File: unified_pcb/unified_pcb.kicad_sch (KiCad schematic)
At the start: 100 parts, among them J1 Conn_01x02_Socket, J2 USB_C_Receptacle, J3 Conn_01x02_Socket, J4 Conn_01x03_Pin, Q1 Q_Photo_NPN, Q2 Q_Photo_NPN, Q3 Q_Photo_NPN, SW1 SW_Push, SW2 SW_Push, U1 BQ27421YZFR-G1A, U10 3.3V LDO, U11 LMD4030T261-OA1, U2 USBLC6-2P6, U4 RP2350_60QFN, U5 TLV7113318DDSER, U6 LP28013HQVF-435, U7 QSPI Flash, U8 TPGLF72101CSP4, U9 ICM-20948, Y1 12MHz

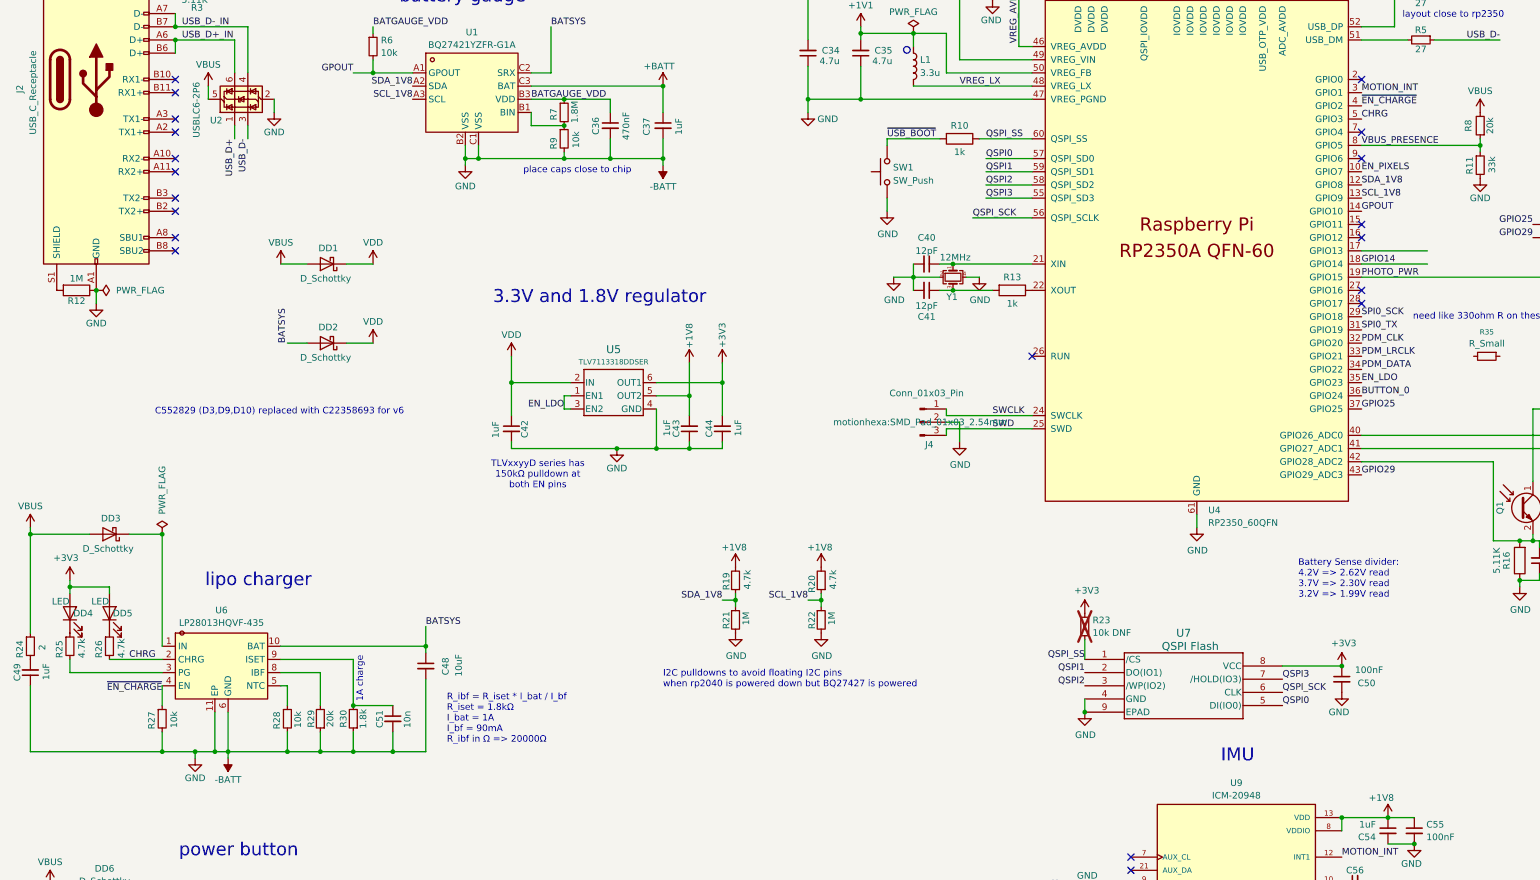
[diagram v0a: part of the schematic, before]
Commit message: switch to LY4176D charger
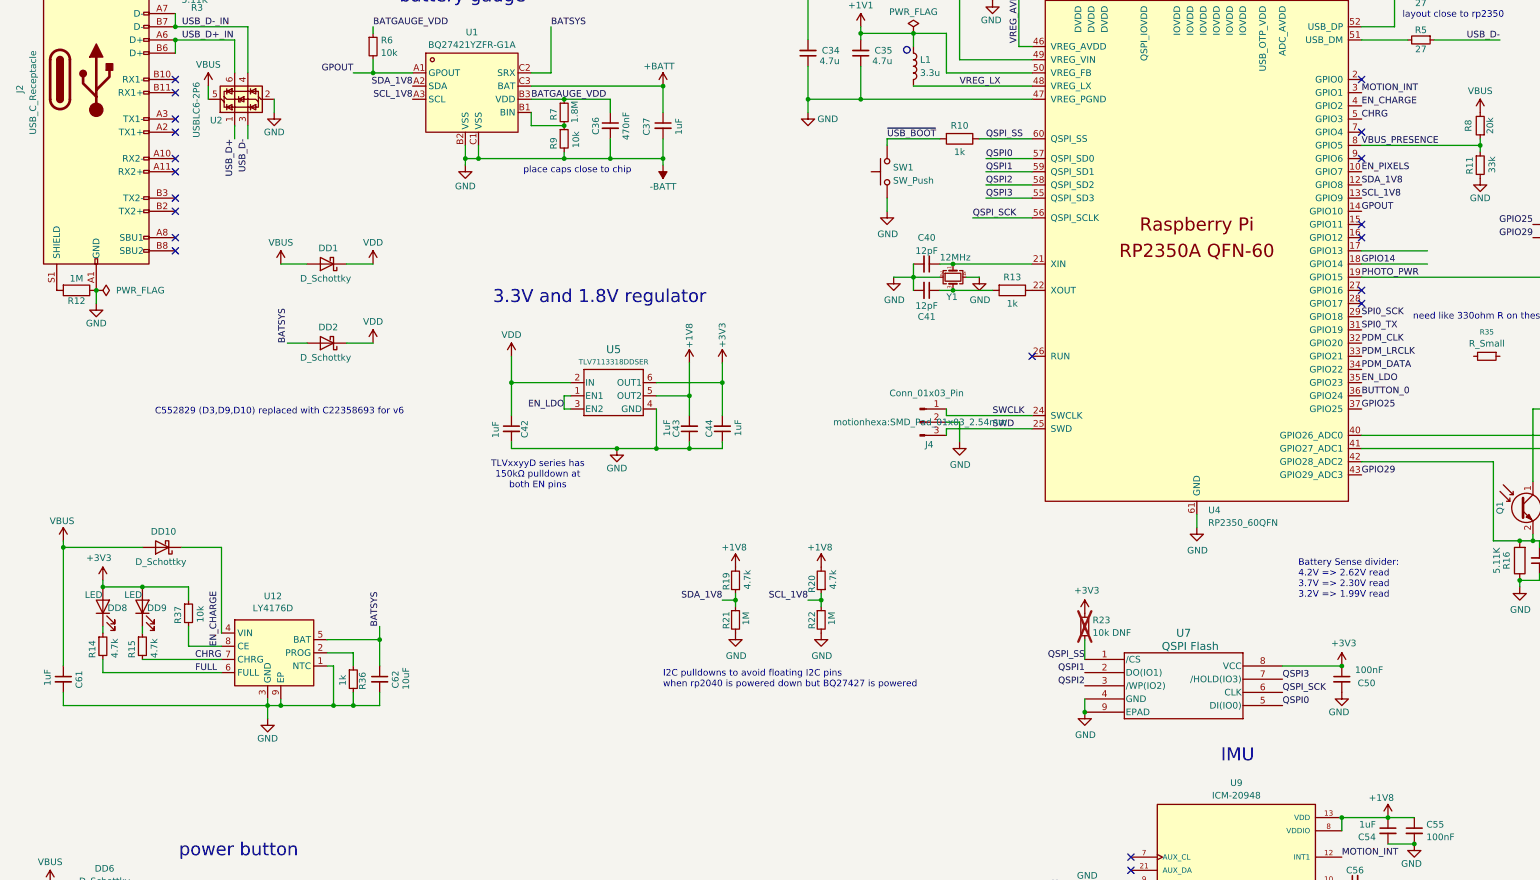
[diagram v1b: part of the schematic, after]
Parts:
- removed C48: 10uF, Capacitor_SMD:C_0603_1608Metric, symbol Device:C_Small
- removed C49: 1uF, Capacitor_SMD:C_0402_1005Metric, symbol Device:C_Small
- removed C51: 10n, Capacitor_SMD:C_0402_1005Metric, symbol Device:C_Small
- removed DD3: D_Schottky, motionhexa:DFN1608D-2, symbol Device:D_Schottky
- removed DD4, DD5: LED, LED_SMD:LED_0402_1005Metric, symbol Device:LED
- removed R24: 2, Resistor_SMD:R_0402_1005Metric, symbol Device:R_Small
- removed R25, R26: 4.7k, Resistor_SMD:R_0402_1005Metric, symbol Device:R_Small
- removed R27, R28: 10k, Resistor_SMD:R_0402_1005Metric, symbol Device:R_Small
- removed R29: 20k, Resistor_SMD:R_0402_1005Metric, symbol Device:R_Small
- removed R30: 1.8k, Resistor_SMD:R_0402_1005Metric, symbol Device:R_Small
- removed U6: LP28013HQVF-435, motionhexa:TDFN-10_L3.0-W3.0-P0.50-BL-EP, symbol motionhexa:LP28013HQVF-435
- added C61: 1uF, Capacitor_SMD:C_0402_1005Metric, symbol Device:C_Small
- added C62: 10uF, Capacitor_SMD:C_0603_1608Metric, symbol Device:C_Small
- added DD10: D_Schottky, motionhexa:DFN1608D-2, symbol Device:D_Schottky
- added DD8, DD9: LED, LED_SMD:LED_0402_1005Metric, symbol Device:LED
- added R14, R15: 4.7k, Resistor_SMD:R_0402_1005Metric, symbol Device:R_Small
- added R36: 1k, Resistor_SMD:R_0402_1005Metric, symbol Device:R_Small
- added R37: 10k, Resistor_SMD:R_0402_1005Metric, symbol Device:R_Small
- added U12: LY4176D, Package_DFN_QFN:DFN-8-1EP_2x2mm_P0.5mm_EP0.6x1.2mm, symbol motionhexa:LY4176D
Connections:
- net +3V3: now also DD8.2 (A), DD9.2 (A), R37.1
- net -BATT: now also C61.2, C62.2, R36.2, U12.1 (NTC), U12.3 (GND), U12.9 (EP)
- net BATSYS: now also C62.1, U12.5 (BAT)
- net CHRG: now also R15.2, U12.7 (CHRG)
- net VBUS: now also C61.1, DD10.2 (A)
- net ~{EN_CHARGE} renamed EN_CHARGE
- net EN_CHARGE: now also R37.2, U12.8 (CE)
- new net: DD9.1 (K), R15.1
- new net: DD10.1 (K), U12.4 (VIN)
- new net: DD8.1 (K), R14.1
- new net: R36.1, U12.2 (PROG)
- new net FULL: R14.2, U12.6 (FULL)
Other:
- note removed: "1A charge"
- note removed: "R_ibf = R_iset * I_bat / I_bf R_iset = 1.8kΩ I_bat = 1A I_bf = 90mA R_ibf in Ω => 20000Ω"
- note removed: "lipo charger"

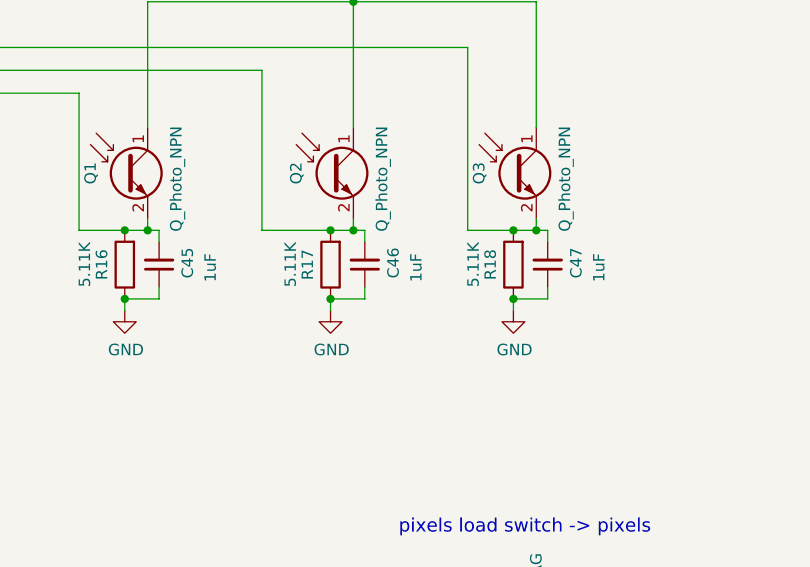
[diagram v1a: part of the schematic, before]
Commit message: phototransistor caps to 470nF for faster sampling
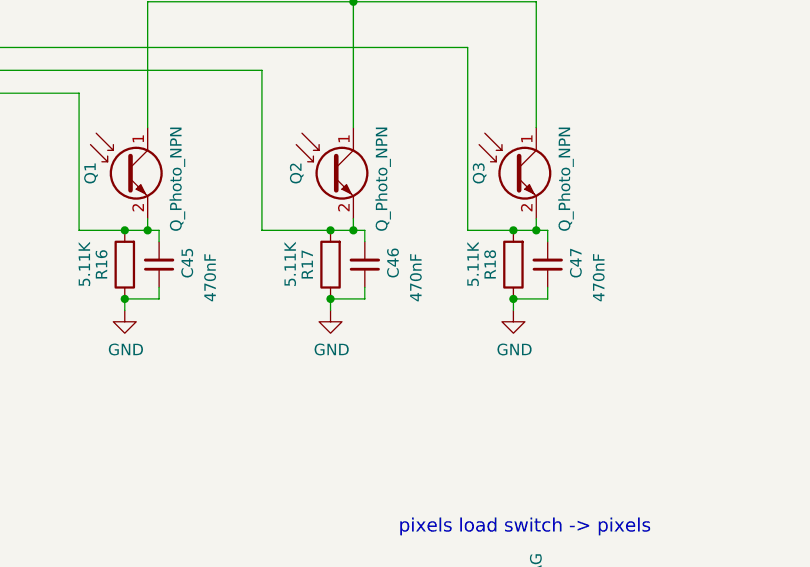
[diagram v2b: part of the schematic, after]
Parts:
- C45, C46, C47: value 1uF -> 470nF; Designation CL05A105KP5NNNC -> CL05A474KP5NNNC; LCSC C14445 -> C47339
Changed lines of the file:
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@@
 			)
 		)
-		(property "Value" "1uF"
+		(property "Value" "470nF"
 			(at 347.345 160.02 90)
 			(effects
@@
 			)
 		)
-		(property "LCSC" "C14445"
+		(property "LCSC" "C47339"
 			(at 341.63 161.29 0)
 			(effects
@@
 			)
 		)
-		(property "Designation" "CL05A105KP5NNNC"
+		(property "Designation" "CL05A474KP5NNNC"
 			(at 341.63 161.29 0)
 			(effects
@@
 			)
 		)
-		(property "Value" "1uF"
+		(property "Value" "470nF"
 			(at 367.665 160.02 90)
 			(effects
@@
 			)
 		)
-		(property "LCSC" "C14445"
+		(property "LCSC" "C47339"
 			(at 361.95 161.29 0)
 			(effects
@@
 			)
 		)
-		(property "Designation" "CL05A105KP5NNNC"
+		(property "Designation" "CL05A474KP5NNNC"
 			(at 361.95 161.29 0)
 			(effects
@@
 			)
 		)
-		(property "Value" "1uF"
+		(property "Value" "470nF"
 			(at 324.485 160.02 90)
 			(effects
@@
 			)
 		)
-		(property "LCSC" "C14445"
+		(property "LCSC" "C47339"
 			(at 318.77 161.29 0)
 			(effects
@@
 			)
 		)
-		(property "Designation" "CL05A105KP5NNNC"
+		(property "Designation" "CL05A474KP5NNNC"
 			(at 318.77 161.29 0)
 			(effects

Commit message: change BQ27421 back to BQ27427
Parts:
- removed R35: R_Small, symbol Device:R_Small
- C36: value 470nF -> 2.2uF; Designation GRM155R61A474KE15D -> CC0402KRX5R6BB225; LCSC C77003 -> C326606
- U1: value BQ27421YZFR-G1A -> BQ27427YZFR; footprint Package_BGA:Texas_DSBGA-9_1.62x1.58mm_Layout3x3_P0.5mm -> Package_BGA:BGA-9_1.6x1.6mm_Layout3x3_P0.5mm; Designation BQ27421YZFR-G1A -> BQ27427YZFR; LCSC C139621 -> C6075475; LCSC Part (none) -> C6075475
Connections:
- net GPIO14: no longer names the net of U4.18 (GPIO14)
- no-connect marks 21 -> 23
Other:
- note removed: "FIXME: can this go back to BQ27427?"
- moved on the sheet: C40, C41

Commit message: add an RS0302 for dual-voltage-zone i2c; sprinkle some RC in various places for good measure; lots of layout improvements
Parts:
- added C38: 100nF, Capacitor_SMD:C_0402_1005Metric, symbol Device:C_Small
- added C39: 4.7uF, Capacitor_SMD:C_0402_1005Metric, symbol Device:C_Small
- added R24: 1k, Resistor_SMD:R_0402_1005Metric, symbol Device:R
- added R25: 200k, Resistor_SMD:R_0402_1005Metric, symbol Device:R_Small
- added R26, R27: 4.7k, Resistor_SMD:R_0402_1005Metric, symbol Device:R_Small
- added U3: RS0302, Package_SON:X2SON-8_1.4x1mm_P0.35mm, symbol motionhexa:RS0302
- C22: value 4.7u -> 4.7uF
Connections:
- net +1V8: now also R26.2, R27.2, U3.2 (VREF1); no longer R19.2, R20.2
- net +3V3: now also R19.2, R20.2, R25.2
- net -BATT: now also C38.1, C39.1, U3.1 (GND)
- net BUTTON_0: now also R24.1; no longer U4.36 (GPIO24)
- net CHRG: no longer U4.5 (GPIO3)
- net EN_PIXELS: now also U4.15 (GPIO11); no longer U4.10 (GPIO7)
- net GPOUT: now also U4.16 (GPIO12); no longer U4.14 (GPIO10)
- net MOTION_INT: now also U4.2 (GPIO0); no longer U4.3 (GPIO1)
- net SCL_1V8: now also R27.1, U3.4 (SDA1); no longer R20.1, R22.1, U1.A3 (SCL), U4.13 (GPIO9)
- net SDA_1V8: now also R26.1, U3.3 (SCL1); no longer R19.1, R21.1, U1.A2 (SDA), U4.12 (GPIO8)
- net VBUS: now also C39.2; no longer C61.1
- net VBUS_PRESENCE: now also U4.14 (GPIO10); no longer U4.8 (GPIO5)
- net at DD10.1 (K), U12.4 (VIN): now also C61.1
- new net: C38.2, R25.1, U3.7 (VREF2), U3.8 (EN)
- new net: R24.2, U4.36 (GPIO24)
- new net SCL_3V3: R20.1, R22.1, U1.A3 (SCL), U3.5 (SDA2), U4.13 (GPIO9)
- new net SDA_3V3: R19.1, R21.1, U1.A2 (SDA), U3.6 (SCL2), U4.12 (GPIO8)
- no-connect marks 23 -> 24
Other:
- note added: "CHECK TAPE ORIENTATION"
- note added: "I2C"
- note added: "I2C pulldown avoids floating I2C when BQ27427 is powered but RP2350 is not"
- note added: "SDA/SCL swapped for U3 layout"
- note removed: "I2C pulldowns to avoid floating I2C pins when rp2040 is powered down but BQ27427 is powered"
- moved on the sheet: DD10, J3, R11, R19, R20, R21, R22, R8
